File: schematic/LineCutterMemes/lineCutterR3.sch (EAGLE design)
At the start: 62 parts, among them IC2 MC33269ST-3.3T3, J1 10118192-0001LF, Q1 AO4576, Q2 AO4576, Q4 AO4576, Q5 DMG2305, SW1 KMR2, U1 MS560702BA03-50, U2 MDBT50Q, U3 S25FL128SDPMFIG13S03016, U4 ACS711KEXLT-15AB-T, U6 ICM-20602, X1 2x5 0.05", Y2 32.768

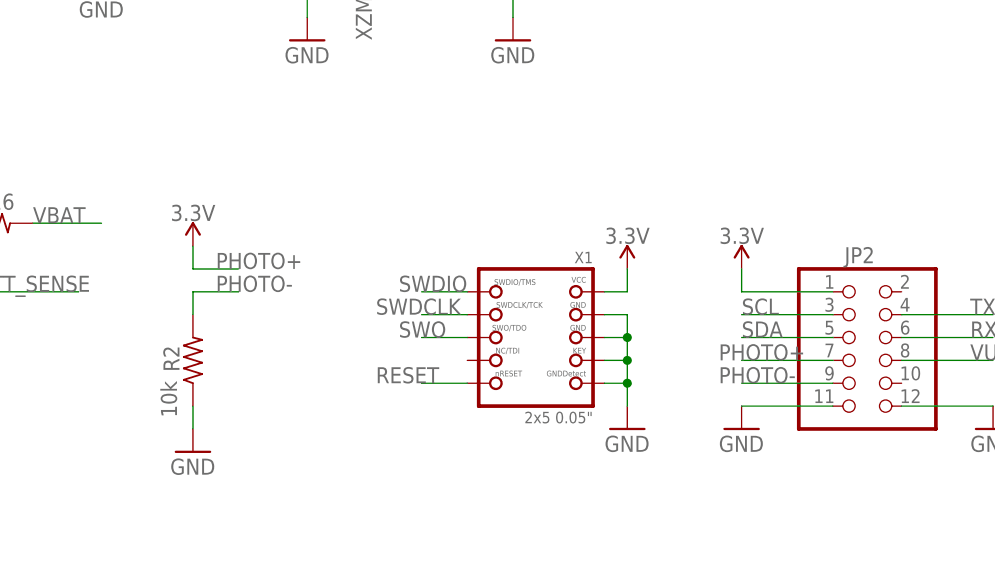
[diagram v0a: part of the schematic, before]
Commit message: Fix photoresistor header
Photo+ was not connected to 3v3
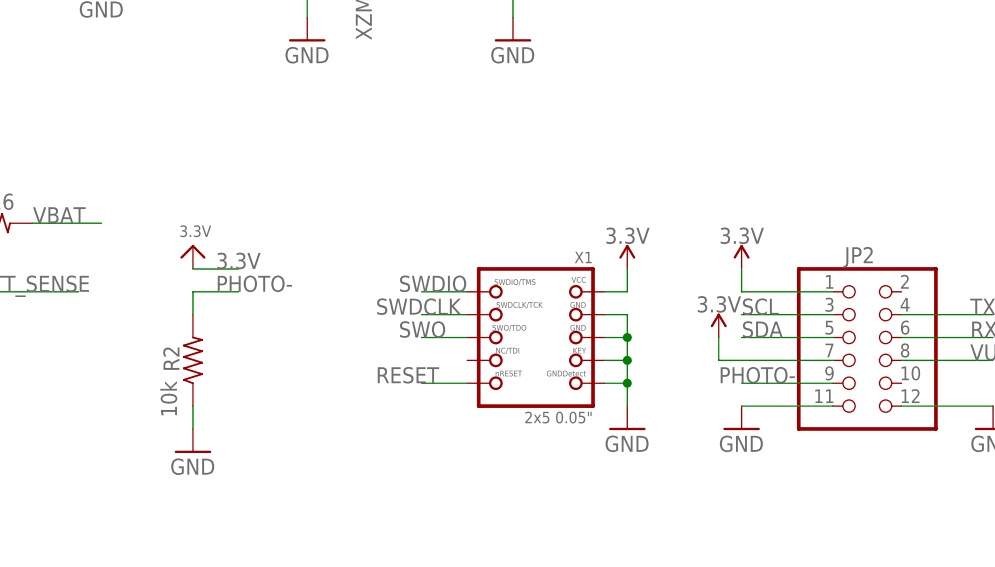
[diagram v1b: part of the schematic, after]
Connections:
- removed net PHOTO+: JP2.7
- net 3.3V: now also JP2.7
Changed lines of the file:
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@@
 <part name="C2" library="rcl" library_urn="urn:adsk.eagle:library:334" deviceset="C-EU" device="C0805" package3d_urn="urn:adsk.eagle:package:23617/2" value="22pF"/>
 <part name="C3" library="rcl" library_urn="urn:adsk.eagle:library:334" deviceset="C-EU" device="C0805" package3d_urn="urn:adsk.eagle:package:23617/2" value="22pF"/>
-<part name="SUPPLY2" library="SparkFun-PowerSymbols" deviceset="3.3V" device=""/>
 <part name="R2" library="rcl" library_urn="urn:adsk.eagle:library:334" deviceset="R-US_" device="R0805" package3d_urn="urn:adsk.eagle:package:23553/2" value="10k"/>
 <part name="GND20" library="supply1" library_urn="urn:adsk.eagle:library:371" deviceset="GND" device=""/>
 <part name="IC2" library="linear" library_urn="urn:adsk.eagle:library:262" deviceset="MC33269ST*" device="" package3d_urn="urn:adsk.eagle:package:28541/2" technology="-3.3T3"/>
 <part name="GND21" library="supply1" library_urn="urn:adsk.eagle:library:371" deviceset="GND" device=""/>
+<part name="U$8" library="microbuilder" deviceset="3.3V" device=""/>
+<part name="SUPPLY2" library="SparkFun-PowerSymbols" deviceset="3.3V" device=""/>
 </parts>
 <sheets>
@@
 <attribute name="VALUE" x="110.51" y="208.04" size="1.27" layer="96" font="vector" rot="R180" align="center"/>
 </instance>
-<instance part="SUPPLY2" gate="G$1" x="187.96" y="139.7" smashed="yes" grouprefs="PHOTORESISTOR">
-<attribute name="VALUE" x="187.96" y="142.494" size="1.778" layer="96" align="bottom-center"/>
-</instance>
 <instance part="R2" gate="G$1" x="187.96" y="127" smashed="yes" rot="R90" grouprefs="PHOTORESISTOR">
 <attribute name="NAME" x="186.4614" y="125.73" size="1.778" layer="95" rot="R90"/>
@@
 <instance part="GND21" gate="1" x="177.8" y="167.64" smashed="yes" grouprefs="3V3">
 <attribute name="VALUE" x="175.26" y="165.1" size="1.778" layer="96"/>
+</instance>
+<instance part="U$8" gate="G$1" x="187.96" y="139.7" smashed="yes">
+<attribute name="VALUE" x="186.436" y="140.716" size="1.27" layer="96"/>
+</instance>
+<instance part="SUPPLY2" gate="G$1" x="246.38" y="129.54" smashed="yes">
+<attribute name="VALUE" x="246.38" y="132.334" size="1.778" layer="96" align="bottom-center"/>
 </instance>
 </instances>
@@
 <junction x="177.8" y="182.88" grouprefs="3V3"/>
 </segment>
+<segment>
+<wire x1="187.96" y1="137.16" x2="193.04" y2="137.16" width="0.1524" layer="91" grouprefs="PHOTORESISTOR"/>
+<label x="190.5" y="137.16" size="1.778" layer="95" grouprefs="PHOTORESISTOR"/>
+<pinref part="U$8" gate="G$1" pin="3.3V"/>
+</segment>
+<segment>
+<pinref part="JP2" gate="A" pin="7"/>
+<wire x1="259.08" y1="127" x2="246.38" y2="127" width="0.1524" layer="91"/>
+<wire x1="246.38" y1="127" x2="246.38" y2="129.54" width="0.1524" layer="91"/>
+<pinref part="SUPPLY2" gate="G$1" pin="3.3V"/>
+</segment>
 </net>
 <net name="N$10" class="0">
@@
 </segment>
 </net>
-<net name="PHOTO+" class="0">
-<segment>
-<pinref part="JP2" gate="A" pin="7"/>
-<wire x1="259.08" y1="127" x2="248.92" y2="127" width="0.1524" layer="91" grouprefs="HEADER"/>
-<label x="246.38" y="127" size="1.778" layer="95" grouprefs="HEADER"/>
-</segment>
-<segment>
-<pinref part="SUPPLY2" gate="G$1" pin="3.3V"/>
-<wire x1="187.96" y1="139.7" x2="187.96" y2="137.16" width="0.1524" layer="91" grouprefs="PHOTORESISTOR"/>
-<wire x1="187.96" y1="137.16" x2="193.04" y2="137.16" width="0.1524" layer="91" grouprefs="PHOTORESISTOR"/>
-<label x="190.5" y="137.16" size="1.778" layer="95" grouprefs="PHOTORESISTOR"/>
-</segment>
-</net>
